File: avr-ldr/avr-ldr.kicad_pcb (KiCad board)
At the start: 2 copper layers, 54.6 x 35.6 mm, 26 parts, among them CON1 AVR-ISP-6, IC1 ATTINY2313-P, P1 RJ11, P2 CONN_01X05, U1 PCA82C250, Y1 4MHz

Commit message: Attempt #2 at my PCB design
Guess I may actually create this one?!
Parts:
- added REF**: 1pin, Connect:1pin, F.Cu at (116.8, 144.8)
- added REF**: 1pin, Connect:1pin, F.Cu at (116.8, 123.2)
- C3, C5, R7: moved to B.Cu
- R1: moved to F.Cu
- moved C6 45.9 mm to (131.4, 142.2)
- moved R9 43.4 mm to (142.9, 147.3), turned to 0 degrees
- moved D2 42.8 mm to (146.7, 147.3), turned to 0 degrees
- moved CON1 42.5 mm to (144.8, 121.9), turned to 270 degrees
- moved C3 41.7 mm to (154.9, 132.1), turned to 270 degrees
- moved R2 38.4 mm to (129.5, 148.0), turned to 0 degrees
- moved R7 37.1 mm to (134.6, 125.7)
- moved RV1 36.4 mm to (126.4, 119.4)
- moved R8 36.2 mm to (142.9, 143.5), turned to 0 degrees
- moved IC1 35.6 mm to (151.1, 123.2), turned to 0 degrees
- moved D1 35.5 mm to (146.7, 143.5), turned to 0 degrees
- moved R5 31.4 mm to (137.2, 139.7)
- moved Y1 30.6 mm to (144.1, 133.3), turned to 90 degrees
- moved P2 30.6 mm to (135.9, 144.8), turned to 270 degrees
- moved C2 29.1 mm to (147.3, 135.9), turned to 90 degrees
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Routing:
- net GND: track 142.8 -> 114.4 mm, vias 4 -> 1
- net Net-(IC1-Pad13): track 34.9 -> 53.0 mm
- net LDR_OUT: track 28.1 -> 37.7 mm
- net SCK: track 13.0 -> 22.5 mm
- net AVR_RXD: track 7.46 -> 16.7 mm
- net AVR_TXD: track 13.2 -> 21.3 mm, vias 0 -> 1
- net INPUT_A: track 18.1 -> 25.9 mm
- net INPUT_B: track 18.1 -> 25.7 mm, vias 0 -> 2
- net Net-(P1-Pad1): track 10.8 -> 5.22 mm, vias 1 -> 0
- net MOSI: track 14.7 -> 20.1 mm
- net Net-(D1-Pad2): track 9.78 -> 5.13 mm
- net VCC: track 81.0 -> 84.8 mm, vias 1 -> 2
- net Net-(C5-Pad2): track 29.9 -> 32.5 mm
- net Net-(C1-Pad1): track 8.99 -> 6.98 mm
- net Net-(P1-Pad5): track 8.77 -> 7.16 mm
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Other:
- board size 54.6 x 35.6 mm -> 48.9 x 31.8 mm
- net class Default: clearance 0.1524 -> 0.2; trace_width 0.1524 -> 0.25; via_dia 0.6858 -> 0.6; via_drill 0.3302 -> 0.4
- rule trace_clearance: 0.1524 -> 0.2
- rule trace_min: 0.1524 -> 0.2
- rule via_min_drill: 0.3302 -> 0.3
- rule via_min_size: 0.6858 -> 0.4
- board text added: "V2016.04.23"

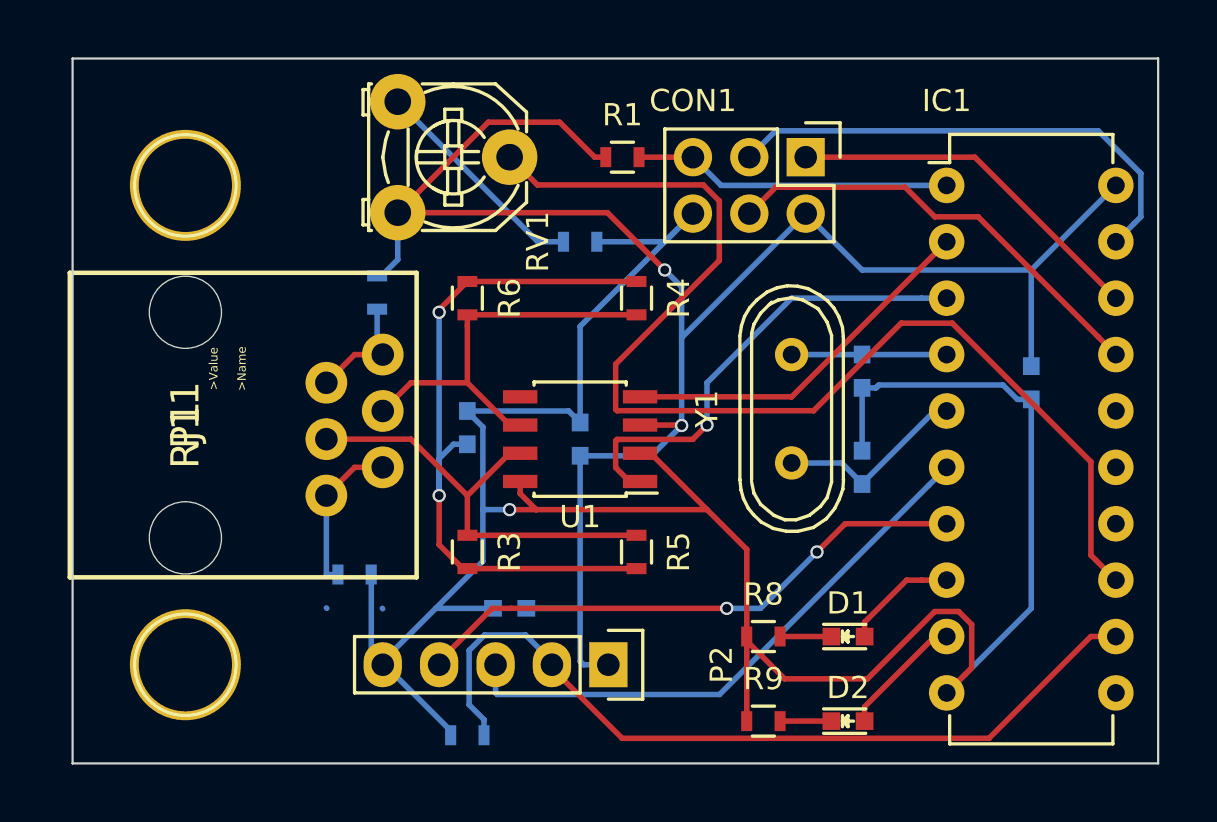
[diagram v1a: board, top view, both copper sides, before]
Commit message: Final changes to PCB (GND copper fill and date update)
Off to OSHPark it has gone!
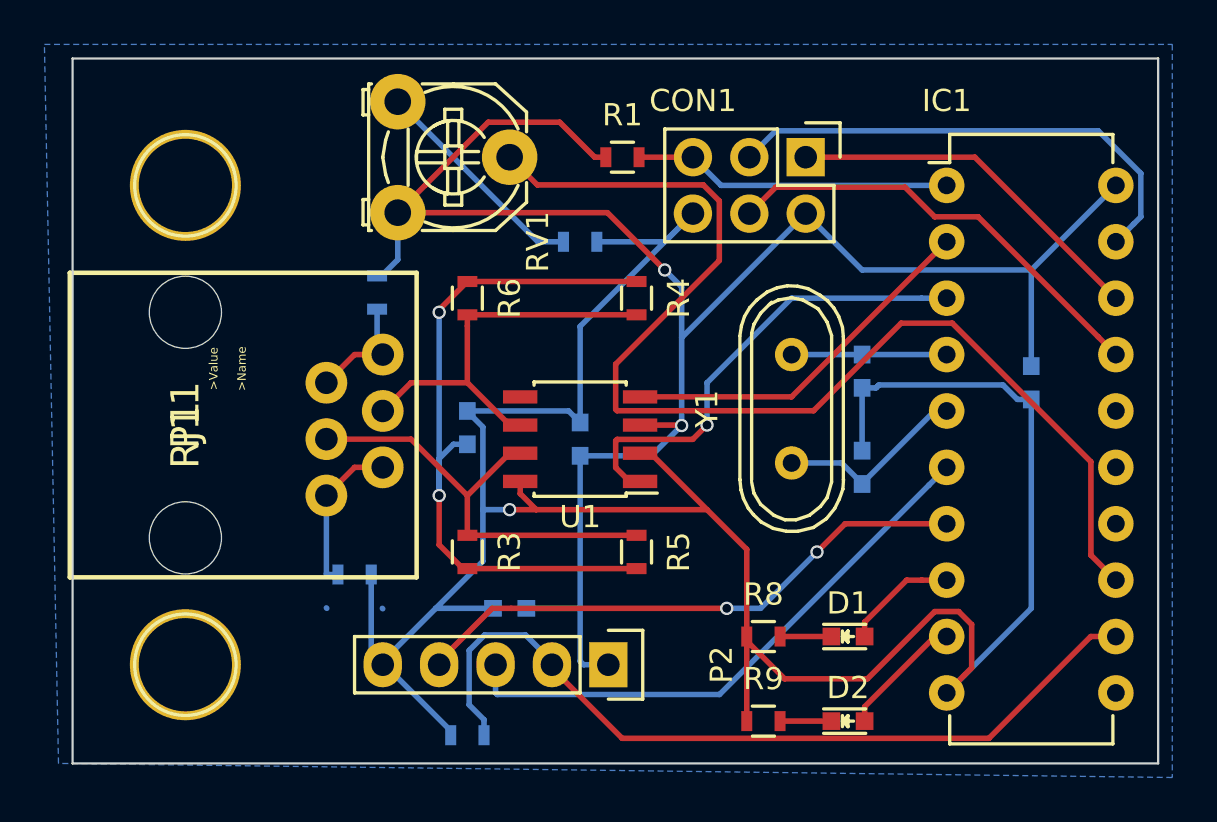
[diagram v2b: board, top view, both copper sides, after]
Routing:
- added copper zone on B.Cu, net GND
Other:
- board text added: "V2016.05.03"
- board text removed: "V2016.04.23"
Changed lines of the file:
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@@
 (kicad_pcb (version 4) (host pcbnew 4.0.2+dfsg1-stable)
   (general
-    (links 0)
+    (links 59)
     (no_connects 0)
-    (area 108.410399 117.424999 160.705001 150.195)
+    (area 111.709999 117.424999 160.705001 149.275001)
     (thickness 1.6)
     (drawings 5)
@@
     (pad 1 thru_hole circle (at 0 0) (size 5 5) (drill 4.2) (layers *.Cu *.Mask F.SilkS))
   )
-  (gr_text V2016.04.23 (at 152.908 119.38) (layer B.SilkS)
+  (gr_text V2016.05.03 (at 152.908 119.38) (layer B.SilkS)
     (effects (font (size 1.5 1.5) (thickness 0.3)) (justify mirror))
   )
@@
   (gr_line (start 111.76 117.475) (end 160.655 117.475) (layer Edge.Cuts) (width 0.1))
   (gr_line (start 111.76 149.225) (end 111.76 117.475) (layer Edge.Cuts) (width 0.1))
+  (segment (start 125.73 142.26) (end 125.71 142.24) (width 0.25) (layer B.Cu) (net 0))
+  (segment (start 123.19 142.22) (end 123.21 142.24) (width 0.25) (layer B.Cu) (net 0))
   (segment (start 147.32 130.81) (end 144.145 130.81) (width 0.25) (layer B.Cu) (net 1))
   (segment (start 151.13 130.81) (end 147.32 130.81) (width 0.25) (layer B.Cu) (net 1))
@@
   (segment (start 135.37 125.73) (end 138.43 125.73) (width 0.25) (layer B.Cu) (net 2))
   (segment (start 138.43 125.73) (end 139.7 124.46) (width 0.25) (layer B.Cu) (net 2))
-  (segment (start 125.73 142.26) (end 125.71 142.24) (width 0.25) (layer B.Cu) (net 2))
   (segment (start 129.54 133.35) (end 129.54 133.375) (width 0.25) (layer B.Cu) (net 2))
   (segment (start 129.54 133.375) (end 130.240001 134.075001) (width 0.25) (layer B.Cu) (net 2))
@@
   (segment (start 123.19 140.696) (end 123.21 140.716) (width 0.25) (layer B.Cu) (net 27))
   (segment (start 123.21 140.716) (end 123.71 140.716) (width 0.25) (layer B.Cu) (net 27))
-  (segment (start 123.19 142.22) (end 123.21 142.24) (width 0.25) (layer B.Cu) (net 27))
   (segment (start 123.19 137.16) (end 124.46 135.89) (width 0.25) (layer F.Cu) (net 27))
   (segment (start 124.46 135.89) (end 125.73 135.89) (width 0.25) (layer F.Cu) (net 27))
   (segment (start 133.87 125.73) (end 132.715 125.73) (width 0.25) (layer B.Cu) (net 28))
   (segment (start 132.715 125.73) (end 126.40564 119.42064) (width 0.25) (layer B.Cu) (net 28))
+  (zone (net 2) (net_name GND) (layer B.Cu) (hatch edge 0.508)
+    (connect_pads (clearance 0.508))
+    (min_thickness 0.254)
+    (fill yes (arc_segments 16) (thermal_gap 0.508) (thermal_bridge_width 0.508))
+    (polygon
+      (pts
+        (xy 110.49 116.84) (xy 161.29 116.84) (xy 161.29 149.86) (xy 111.125 149.225)
+      )
+    )
+  )
 )
